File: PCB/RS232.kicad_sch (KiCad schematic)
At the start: 5 parts, among them IC45 MAX232IDR

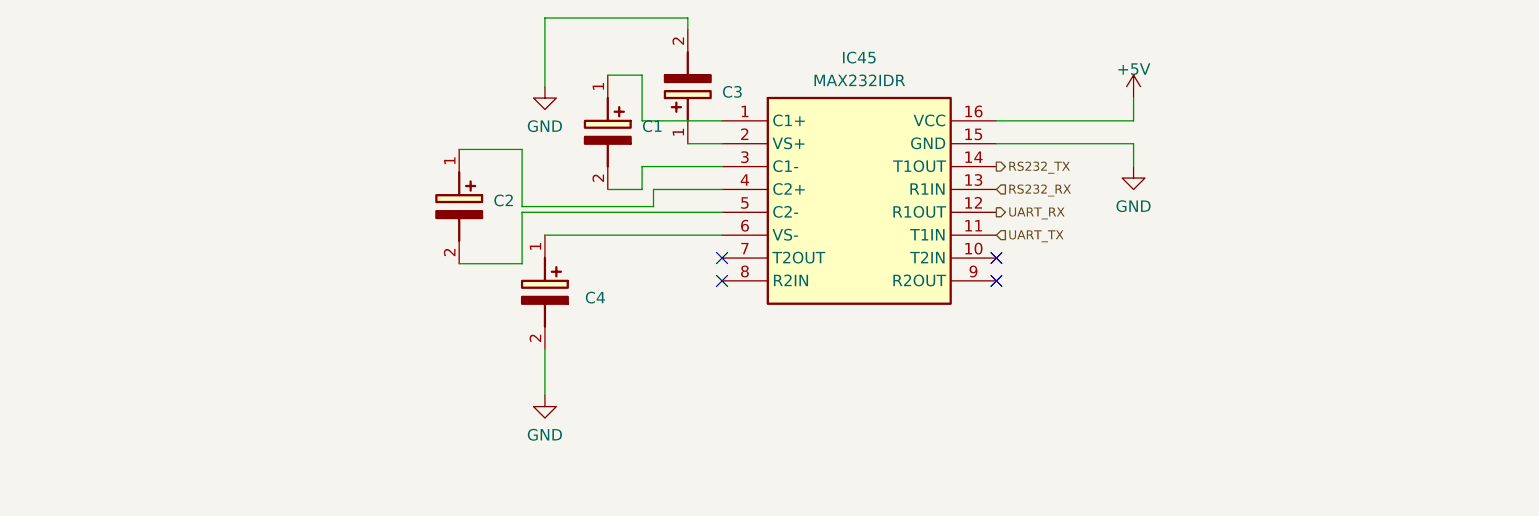
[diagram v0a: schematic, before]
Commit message: Redesigned, to utilize the ESP32 as the basis
* Implemented EEPROM
* Implemented RTC
* Implemented RS232 and 485
* Implemented CANBus
* Implemented everything
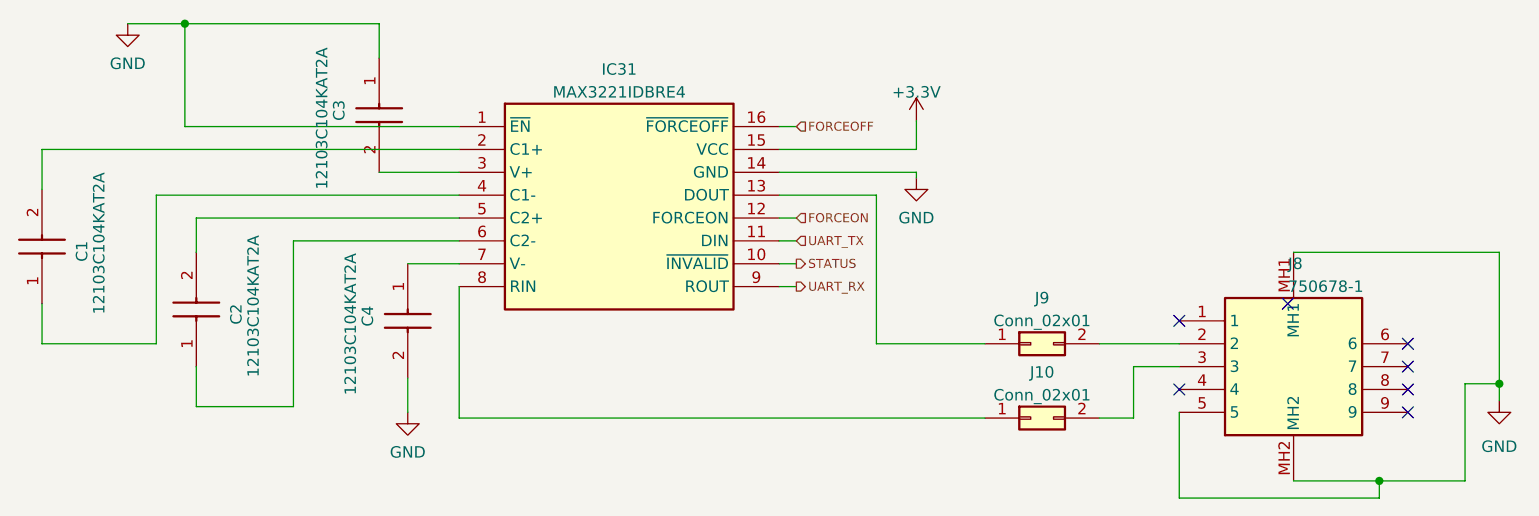
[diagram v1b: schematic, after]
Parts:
- removed C1, C2, C3, C4: 865060640001, CAPAE430X550N, symbol 865060640001:865060640001
- removed IC45: MAX232IDR, SOIC127P600X175-16N, symbol MAX232IDR:MAX232IDR
- added C1, C2, C3, C4: 12103C104KAT2A, 12103C104KAT2A:CAPC3325X94N, symbol 12103C104KAT2A:12103C104KAT2A
- added IC31: MAX3221IDBRE4, MAX3221IDBRE4:SOP65P780X200-16N, symbol MAX3221IDBRE4:MAX3221IDBRE4
- added J10, J9: Conn_02x01, Connector_PinHeader_2.54mm:PinHeader_2x01_P2.54mm_Horizontal, symbol Connector_Generic:Conn_02x01
- added J8: 750678-1, 750678-1:7506781, symbol 750678-1:750678-1
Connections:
- net GND: now also C3.1, C4.2, IC31.1 (~{EN}), IC31.14 (GND), J8.5, J8.MH1, J8.MH2
- net UART_RX: now also IC31.9 (ROUT)
- net UART_TX: now also IC31.11 (DIN)
- new net: C3.2, IC31.3 (V+)
- new net: C1.1, IC31.4 (C1-)
- new net: C1.2, IC31.2 (C1+)
- new net: J8.2, J9.2 (Pin_2)
- new net: J10.2 (Pin_2), J8.3
- new net: C4.1, IC31.7 (V-)
- new net: IC31.13 (DOUT), J9.1 (Pin_1)
- new net: C2.2, IC31.5 (C2+)
- new net: C2.1, IC31.6 (C2-)
- new net: IC31.8 (RIN), J10.1 (Pin_1)
- new net +3.3V: IC31.15 (VCC)
- new net FORCEOFF: IC31.16 (~{FORCEOFF})
- new net FORCEON: IC31.12 (FORCEON)
- new net STATUS: IC31.10 (~{INVALID})
- no-connect marks 4 -> 7
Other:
- company: (none) -> UPB - FIIR - Roboți și sisteme de producție

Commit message: Implemented Output block in PCB Started implementation of Input block in PCB
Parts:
- J10, J9: footprint Connector_PinHeader_2.54mm:PinHeader_2x01_P2.54mm_Horizontal -> Connector_PinHeader_2.54mm:PinHeader_2x01_P2.54mm_Vertical
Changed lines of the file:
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@@
       (effects (font (size 1.27 1.27)))
     )
-    (property "Footprint" "Connector_PinHeader_2.54mm:PinHeader_2x01_P2.54mm_Horizontal" (at 162.56 127.635 0)
+    (property "Footprint" "Connector_PinHeader_2.54mm:PinHeader_2x01_P2.54mm_Vertical" (at 162.56 127.635 0)
       (effects (font (size 1.27 1.27)) hide)
     )
@@
       (effects (font (size 1.27 1.27)))
     )
-    (property "Footprint" "Connector_PinHeader_2.54mm:PinHeader_2x01_P2.54mm_Horizontal" (at 162.56 119.38 0)
+    (property "Footprint" "Connector_PinHeader_2.54mm:PinHeader_2x01_P2.54mm_Vertical" (at 162.56 119.38 0)
       (effects (font (size 1.27 1.27)) hide)
     )
